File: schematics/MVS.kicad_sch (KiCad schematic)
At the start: 0 parts

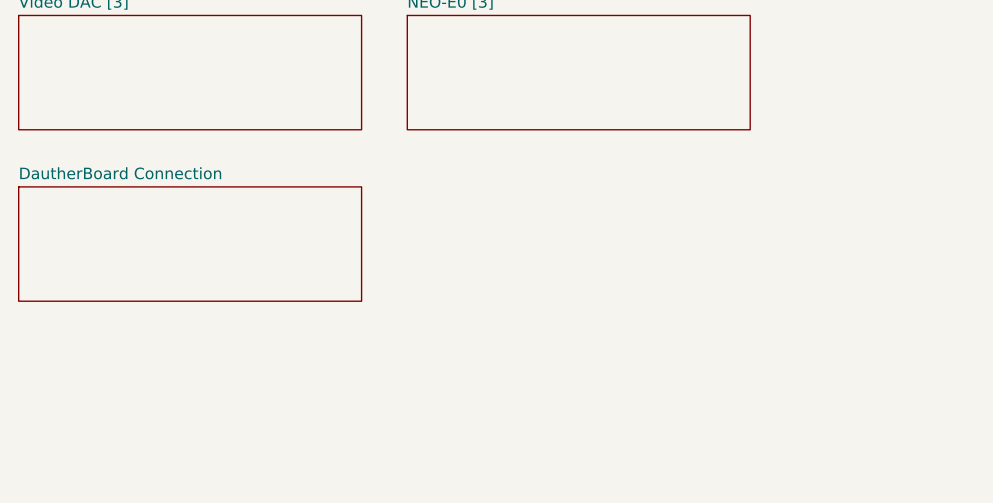
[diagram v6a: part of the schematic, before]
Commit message: complete DaughterBoard
rename sub files
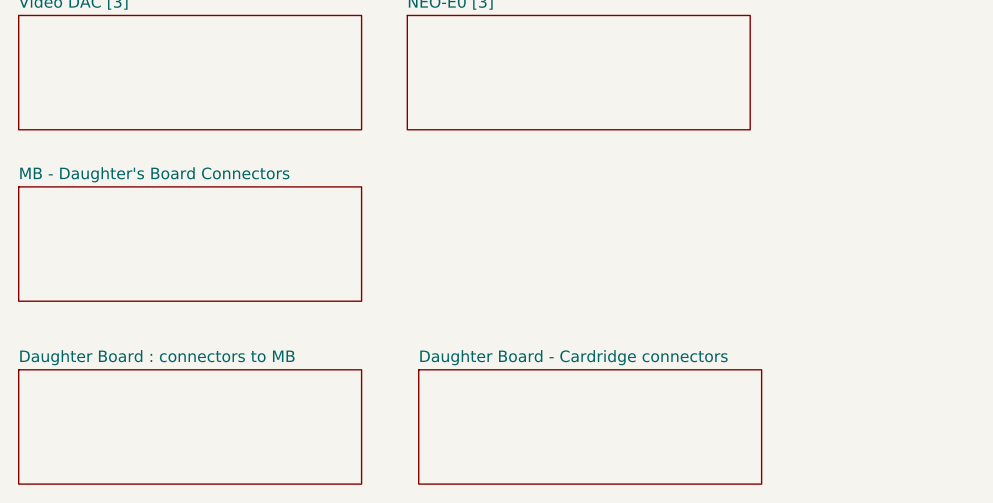
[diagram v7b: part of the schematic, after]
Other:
- sheet DautherBoard Connection renamed MB - Daughter's Board Connectors
- added sheet Daughter Board - Cardridge connectors (DB-Cardridge_Connectors.kicad_sch)
- added sheet Daughter Board : connectors to MB (daughterboard-MB-Connectors.kicad_sch)
- sheet 68K-SP ROM-Work & Back RAM [1]: file 68KWBRAM.kicad_sch -> MV1F-MB-68KWBRAM.kicad_sch
- sheet Audio [4]: file Audio.kicad_sch -> MV1F-MB-Audio.kicad_sch
- sheet Battery Circuit [1]: file BatterySaved.kicad_sch -> MV1F-MB-BatterySaved.kicad_sch
- sheet LSPC2-A2 & VRAM [3]: file lspc2-Vram.kicad_sch -> MV1F-MB-lspc2-Vram.kicad_sch
- sheet MB - Daughter's Board Connectors: file DaughterBoard.kicad_sch -> MV1F-MB-DB-Connectors.kicad_sch
- sheet NEO-C1 Players Input [1]: file PlayersInput.kicad_sch -> MV1F-MB-PlayersInput.kicad_sch
- sheet NEO-E0 [3]: file neo-e0-stuff.kicad_sch -> MV1F-MB-neo-e0-stuff.kicad_sch
- sheet UPD4990 Clock [1]: file clock.kicad_sch -> MV1F-MB-clock.kicad_sch
- sheet Video DAC [3]: file RGBDAC.kicad_sch -> MV1F-MB-RGBDAC.kicad_sch
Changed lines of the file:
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@@
       (effects (font (size 1.27 1.27)) (justify left bottom))
     )
-    (property "Sheetfile" "RGBDAC.kicad_sch" (at 25.4 88.2146 0)
+    (property "Sheetfile" "MV1F-MB-RGBDAC.kicad_sch" (at 25.4 88.2146 0)
       (effects (font (size 1.27 1.27)) (justify left top) hide)
     )
@@
       (effects (font (size 1.27 1.27)) (justify left bottom))
     )
-    (property "Sheetfile" "68KWBRAM.kicad_sch" (at 25.4 31.0646 0)
+    (property "Sheetfile" "MV1F-MB-68KWBRAM.kicad_sch" (at 25.4 31.0646 0)
       (effects (font (size 1.27 1.27)) (justify left top) hide)
     )
@@
       (effects (font (size 1.27 1.27)) (justify left bottom))
     )
-    (property "Sheetfile" "clock.kicad_sch" (at 25.4 69.1646 0)
+    (property "Sheetfile" "MV1F-MB-clock.kicad_sch" (at 25.4 69.1646 0)
       (effects (font (size 1.27 1.27)) (justify left top) hide)
     )
@@
       (effects (font (size 1.27 1.27)) (justify left bottom))
     )
-    (property "Sheetfile" "PlayersInput.kicad_sch" (at 25.4 50.1146 0)
+    (property "Sheetfile" "MV1F-MB-PlayersInput.kicad_sch" (at 25.4 50.1146 0)
       (effects (font (size 1.27 1.27)) (justify left top) hide)
     )
@@
       (project "MVS"
         (path "/8d0803ab-15ed-47a7-8dcb-ab27dc5b29c2" (page "3"))
+      )
+    )
+  )
+  (sheet (at 25.4 114.3) (size 38.1 12.7) (fields_autoplaced)
+    (stroke (width 0.1524) (type solid))
+    (fill (color 0 0 0 0.0000))
+    (property "Sheetname" "Daughter Board : connectors to MB" (at 25.4 113.5884 0)
+      (effects (font (size 1.27 1.27)) (justify left bottom))
+    )
+    (property "Sheetfile" "daughterboard-MB-Connectors.kicad_sch" (at 25.4 127.5846 0)
+      (effects (font (size 1.27 1.27)) (justify left top) hide)
+    )
+    (instances
+      (project "MVS"
+        (path "/8d0803ab-15ed-47a7-8dcb-ab27dc5b29c2" (page "12"))
       )
     )
@@
       (effects (font (size 1.27 1.27)) (justify left bottom))
     )
-    (property "Sheetfile" "lspc2-Vram.kicad_sch" (at 68.58 31.0646 0)
+    (property "Sheetfile" "MV1F-MB-lspc2-Vram.kicad_sch" (at 68.58 31.0646 0)
       (effects (font (size 1.27 1.27)) (justify left top) hide)
     )
@@
       (project "MVS"
         (path "/8d0803ab-15ed-47a7-8dcb-ab27dc5b29c2" (page "8"))
+      )
+    )
+  )
+  (sheet (at 69.85 114.3) (size 38.1 12.7) (fields_autoplaced)
+    (stroke (width 0.1524) (type solid))
+    (fill (color 0 0 0 0.0000))
+    (property "Sheetname" "Daughter Board - Cardridge connectors" (at 69.85 113.5884 0)
+      (effects (font (size 1.27 1.27)) (justify left bottom))
+    )
+    (property "Sheetfile" "DB-Cardridge_Connectors.kicad_sch" (at 69.85 127.5846 0)
+      (effects (font (size 1.27 1.27)) (justify left top) hide)
+    )
+    (instances
+      (project "MVS"
+        (path "/8d0803ab-15ed-47a7-8dcb-ab27dc5b29c2" (page "13"))
       )
     )
@@
       (effects (font (size 1.27 1.27)) (justify left bottom))
     )
-    (property "Sheetfile" "Audio.kicad_sch" (at 113.03 31.0646 0)
+    (property "Sheetfile" "MV1F-MB-Audio.kicad_sch" (at 113.03 31.0646 0) (show_name)
       (effects (font (size 1.27 1.27)) (justify left top) hide)
     )
@@
       (effects (font (size 1.27 1.27)) (justify left bottom))
     )
-    (property "Sheetfile" "BatterySaved.kicad_sch" (at 68.58 69.1646 0)
+    (property "Sheetfile" "MV1F-MB-BatterySaved.kicad_sch" (at 68.58 69.1646 0)
       (effects (font (size 1.27 1.27)) (justify left top) hide)
     )
@@
       (effects (font (size 1.27 1.27)) (justify left bottom))
     )
-    (property "Sheetfile" "neo-e0-stuff.kicad_sch" (at 68.58 88.2146 0)
+    (property "Sheetfile" "MV1F-MB-neo-e0-stuff.kicad_sch" (at 68.58 88.2146 0)
       (effects (font (size 1.27 1.27)) (justify left top) hide)
     )
@@
     (stroke (width 0.1524) (type solid))
     (fill (color 0 0 0 0.0000))
-    (property "Sheetname" "DautherBoard Connection" (at 25.4 93.2684 0)
+    (property "Sheetname" "MB - Daughter's Board Connectors" (at 25.4 93.2684 0)
       (effects (font (size 1.27 1.27)) (justify left bottom))
     )
-    (property "Sheetfile" "DaughterBoard.kicad_sch" (at 25.4 107.2646 0)
+    (property "Sheetfile" "MV1F-MB-DB-Connectors.kicad_sch" (at 25.4 107.2646 0)
       (effects (font (size 1.27 1.27)) (justify left top) hide)
     )

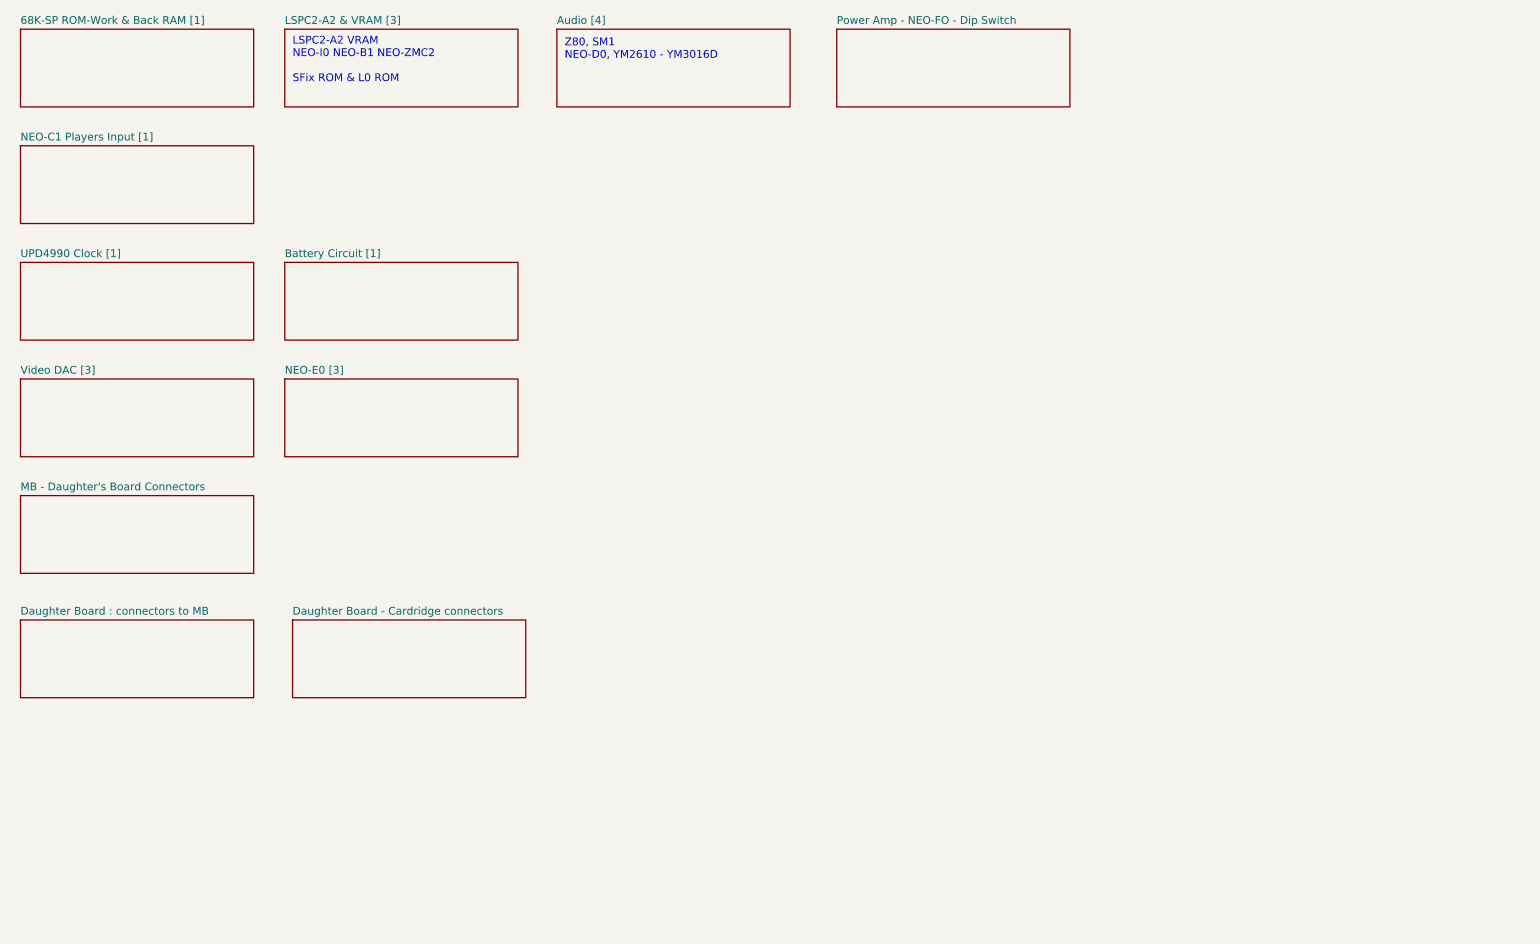
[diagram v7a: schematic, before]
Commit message: Typo... and orphan labels remove
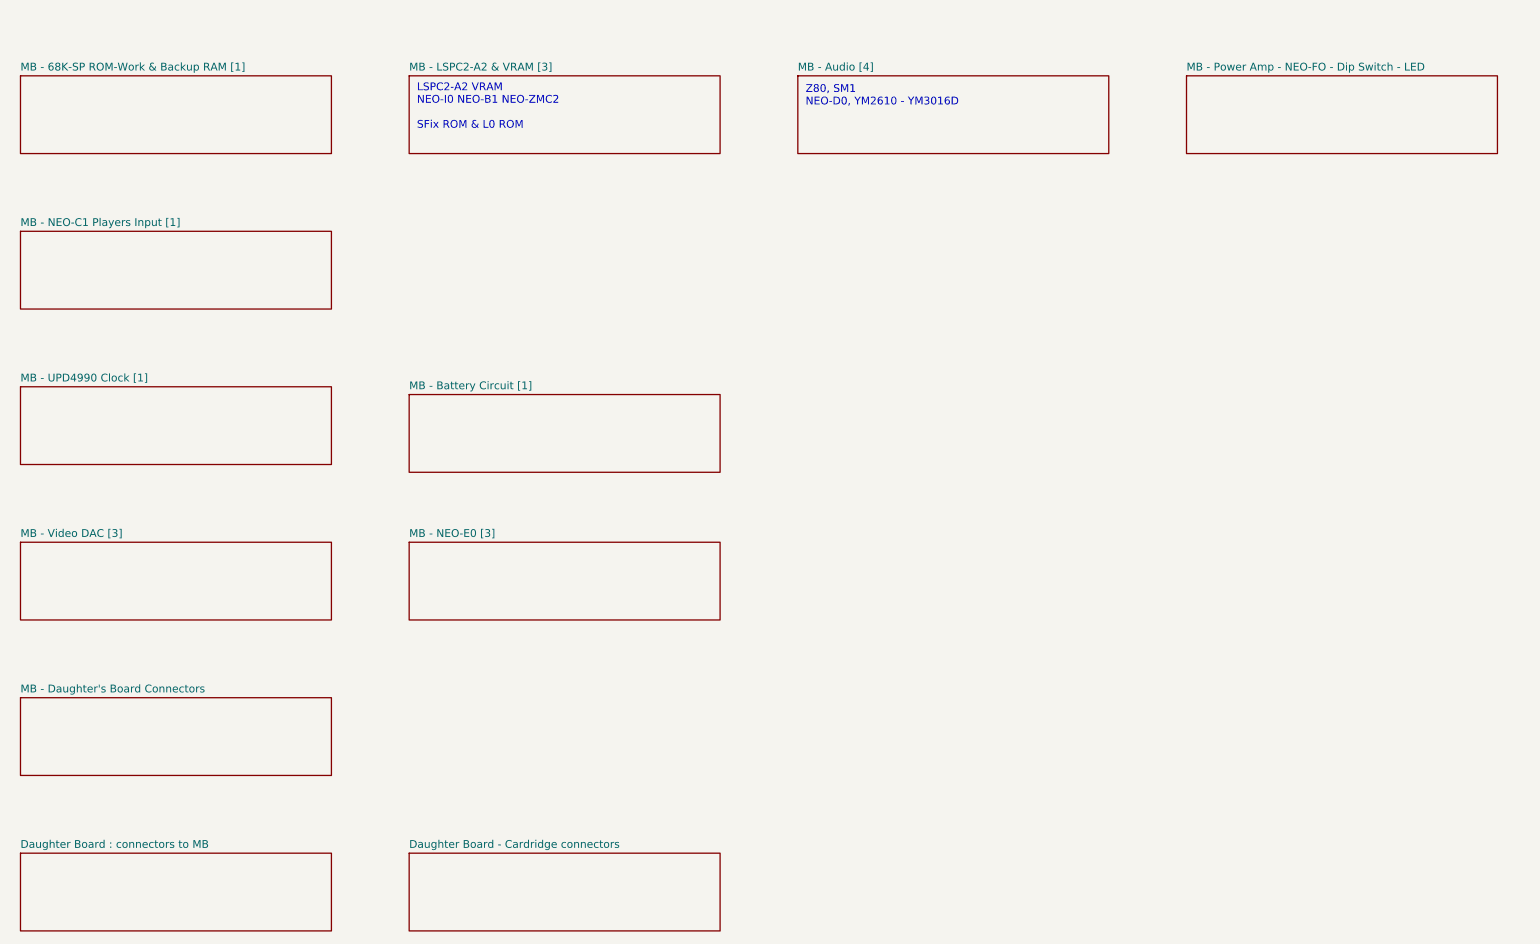
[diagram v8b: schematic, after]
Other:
- sheet 68K-SP ROM-Work & Back RAM [1] renamed MB - 68K-SP ROM-Work & Backup RAM [1]
- sheet Audio [4] renamed MB - Audio [4]
- sheet Battery Circuit [1] renamed MB - Battery Circuit [1]
- sheet LSPC2-A2 & VRAM [3] renamed MB - LSPC2-A2 & VRAM [3]
- sheet NEO-C1 Players Input [1] renamed MB - NEO-C1 Players Input [1]
- sheet NEO-E0 [3] renamed MB - NEO-E0 [3]
- sheet Power Amp - NEO-FO - Dip Switch renamed MB - Power Amp - NEO-FO - Dip Switch - LED
- sheet UPD4990 Clock [1] renamed MB - UPD4990 Clock [1]
- sheet Video DAC [3] renamed MB - Video DAC [3]
- sheet MB - Power Amp - NEO-FO - Dip Switch - LED: file PowerAmp-Neo-FO-Dip.kicad_sch -> MV1F-MB-PowerAmp-Neo-FO-Dip.kicad_sch
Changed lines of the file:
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@@
     (comment 9 "https://github.com/Neo-Geo-Hardwares/Schematics-MV1F")
   )
-  (text "Z80, SM1\nNEO-D0, YM2610 - YM3016D" (at 114.3 22.86 0)
+  (text "Z80, SM1\nNEO-D0, YM2610 - YM3016D" (at 153.67 30.48 0)
     (effects (font (size 1.27 1.27)) (justify left bottom))
   )
   (text "LSPC2-A2 VRAM \nNEO-I0 NEO-B1 NEO-ZMC2 \n\nSFix ROM & L0 ROM"
-    (at 69.85 26.67 0)
+    (at 90.17 34.29 0)
     (effects (font (size 1.27 1.27)) (justify left bottom))
   )
-  (sheet (at 25.4 74.93) (size 38.1 12.7) (fields_autoplaced)
+  (sheet (at 25.4 101.6) (size 50.8 12.7) (fields_autoplaced)
     (stroke (width 0.1524) (type solid))
     (fill (color 0 0 0 0.0000))
-    (property "Sheetname" "Video DAC [3]" (at 25.4 74.2184 0)
+    (property "Sheetname" "MB - Video DAC [3]" (at 25.4 100.8884 0)
       (effects (font (size 1.27 1.27)) (justify left bottom))
     )
-    (property "Sheetfile" "MV1F-MB-RGBDAC.kicad_sch" (at 25.4 88.2146 0)
+    (property "Sheetfile" "MV1F-MB-RGBDAC.kicad_sch" (at 25.4 114.8846 0)
       (effects (font (size 1.27 1.27)) (justify left top) hide)
     )
@@
     )
   )
-  (sheet (at 25.4 17.78) (size 38.1 12.7)
+  (sheet (at 25.4 25.4) (size 50.8 12.7)
     (stroke (width 0.1524) (type solid))
     (fill (color 0 0 0 0.0000))
-    (property "Sheetname" "68K-SP ROM-Work & Back RAM [1]" (at 25.4 17.0684 0)
+    (property "Sheetname" "MB - 68K-SP ROM-Work & Backup RAM [1]" (at 25.4 24.6884 0)
       (effects (font (size 1.27 1.27)) (justify left bottom))
     )
-    (property "Sheetfile" "MV1F-MB-68KWBRAM.kicad_sch" (at 25.4 31.0646 0)
+    (property "Sheetfile" "MV1F-MB-68KWBRAM.kicad_sch" (at 25.4 38.6846 0)
       (effects (font (size 1.27 1.27)) (justify left top) hide)
     )
@@
     )
   )
-  (sheet (at 158.75 17.78) (size 38.1 12.7) (fields_autoplaced)
+  (sheet (at 215.9 25.4) (size 50.8 12.7) (fields_autoplaced)
     (stroke (width 0.1524) (type solid))
     (fill (color 0 0 0 0.0000))
-    (property "Sheetname" "Power Amp - NEO-FO - Dip Switch" (at 158.75 17.0684 0)
+    (property "Sheetname" "MB - Power Amp - NEO-FO - Dip Switch - LED" (at 215.9 24.6884 0)
       (effects (font (size 1.27 1.27)) (justify left bottom))
     )
-    (property "Sheetfile" "PowerAmp-Neo-FO-Dip.kicad_sch" (at 158.75 31.0646 0)
+    (property "Sheetfile" "MV1F-MB-PowerAmp-Neo-FO-Dip.kicad_sch" (at 215.9 38.6846 0)
       (effects (font (size 1.27 1.27)) (justify left top) hide)
     )
@@
     )
   )
-  (sheet (at 25.4 55.88) (size 38.1 12.7) (fields_autoplaced)
+  (sheet (at 25.4 76.2) (size 50.8 12.7) (fields_autoplaced)
     (stroke (width 0.1524) (type solid))
     (fill (color 0 0 0 0.0000))
-    (property "Sheetname" "UPD4990 Clock [1]" (at 25.4 55.1684 0)
+    (property "Sheetname" "MB - UPD4990 Clock [1]" (at 25.4 75.4884 0)
       (effects (font (size 1.27 1.27)) (justify left bottom))
     )
-    (property "Sheetfile" "MV1F-MB-clock.kicad_sch" (at 25.4 69.1646 0)
+    (property "Sheetfile" "MV1F-MB-clock.kicad_sch" (at 25.4 89.4846 0)
       (effects (font (size 1.27 1.27)) (justify left top) hide)
     )
@@
     )
   )
-  (sheet (at 25.4 36.83) (size 38.1 12.7) (fields_autoplaced)
+  (sheet (at 25.4 50.8) (size 50.8 12.7) (fields_autoplaced)
     (stroke (width 0.1524) (type solid))
     (fill (color 0 0 0 0.0000))
-    (property "Sheetname" "NEO-C1 Players Input [1]" (at 25.4 36.1184 0)
+    (property "Sheetname" "MB - NEO-C1 Players Input [1]" (at 25.4 50.0884 0)
       (effects (font (size 1.27 1.27)) (justify left bottom))
     )
-    (property "Sheetfile" "MV1F-MB-PlayersInput.kicad_sch" (at 25.4 50.1146 0)
+    (property "Sheetfile" "MV1F-MB-PlayersInput.kicad_sch" (at 25.4 64.0846 0)
       (effects (font (size 1.27 1.27)) (justify left top) hide)
     )
@@
     )
   )
-  (sheet (at 25.4 114.3) (size 38.1 12.7) (fields_autoplaced)
+  (sheet (at 25.4 152.4) (size 50.8 12.7) (fields_autoplaced)
     (stroke (width 0.1524) (type solid))
     (fill (color 0 0 0 0.0000))
-    (property "Sheetname" "Daughter Board : connectors to MB" (at 25.4 113.5884 0)
+    (property "Sheetname" "Daughter Board : connectors to MB" (at 25.4 151.6884 0)
       (effects (font (size 1.27 1.27)) (justify left bottom))
     )
-    (property "Sheetfile" "daughterboard-MB-Connectors.kicad_sch" (at 25.4 127.5846 0)
+    (property "Sheetfile" "daughterboard-MB-Connectors.kicad_sch" (at 25.4 165.6846 0)
       (effects (font (size 1.27 1.27)) (justify left top) hide)
     )
@@
     )
   )
-  (sheet (at 68.58 17.78) (size 38.1 12.7)
+  (sheet (at 88.9 25.4) (size 50.8 12.7)
     (stroke (width 0.1524) (type solid))
     (fill (color 0 0 0 0.0000))
-    (property "Sheetname" "LSPC2-A2 & VRAM [3]" (at 68.58 17.0684 0)
+    (property "Sheetname" "MB - LSPC2-A2 & VRAM [3]" (at 88.9 24.6884 0)
       (effects (font (size 1.27 1.27)) (justify left bottom))
     )
-    (property "Sheetfile" "MV1F-MB-lspc2-Vram.kicad_sch" (at 68.58 31.0646 0)
+    (property "Sheetfile" "MV1F-MB-lspc2-Vram.kicad_sch" (at 88.9 38.6846 0)
       (effects (font (size 1.27 1.27)) (justify left top) hide)
     )
@@
     )
   )
-  (sheet (at 69.85 114.3) (size 38.1 12.7) (fields_autoplaced)
+  (sheet (at 88.9 152.4) (size 50.8 12.7) (fields_autoplaced)
     (stroke (width 0.1524) (type solid))
     (fill (color 0 0 0 0.0000))
-    (property "Sheetname" "Daughter Board - Cardridge connectors" (at 69.85 113.5884 0)
+    (property "Sheetname" "Daughter Board - Cardridge connectors" (at 88.9 151.6884 0)
       (effects (font (size 1.27 1.27)) (justify left bottom))
     )
-    (property "Sheetfile" "DB-Cardridge_Connectors.kicad_sch" (at 69.85 127.5846 0)
+    (property "Sheetfile" "DB-Cardridge_Connectors.kicad_sch" (at 88.9 165.6846 0)
       (effects (font (size 1.27 1.27)) (justify left top) hide)
     )
@@
     )
   )
-  (sheet (at 113.03 17.78) (size 38.1 12.7) (fields_autoplaced)
+  (sheet (at 152.4 25.4) (size 50.8 12.7) (fields_autoplaced)
     (stroke (width 0.1524) (type solid))
     (fill (color 0 0 0 0.0000))
-    (property "Sheetname" "Audio [4]" (at 113.03 17.0684 0)
+    (property "Sheetname" "MB - Audio [4]" (at 152.4 24.6884 0)
       (effects (font (size 1.27 1.27)) (justify left bottom))
     )
-    (property "Sheetfile" "MV1F-MB-Audio.kicad_sch" (at 113.03 31.0646 0) (show_name)
+    (property "Sheetfile" "MV1F-MB-Audio.kicad_sch" (at 152.4 38.6846 0) (show_name)
       (effects (font (size 1.27 1.27)) (justify left top) hide)
     )
@@
     )
   )
-  (sheet (at 68.58 55.88) (size 38.1 12.7) (fields_autoplaced)
+  (sheet (at 88.9 77.47) (size 50.8 12.7) (fields_autoplaced)
     (stroke (width 0.1524) (type solid))
     (fill (color 0 0 0 0.0000))
-    (property "Sheetname" "Battery Circuit [1]" (at 68.58 55.1684 0)
+    (property "Sheetname" "MB - Battery Circuit [1]" (at 88.9 76.7584 0)
       (effects (font (size 1.27 1.27)) (justify left bottom))
     )
-    (property "Sheetfile" "MV1F-MB-BatterySaved.kicad_sch" (at 68.58 69.1646 0)
+    (property "Sheetfile" "MV1F-MB-BatterySaved.kicad_sch" (at 88.9 90.7546 0)
       (effects (font (size 1.27 1.27)) (justify left top) hide)
     )
@@
     )
   )
-  (sheet (at 68.58 74.93) (size 38.1 12.7) (fields_autoplaced)
+  (sheet (at 88.9 101.6) (size 50.8 12.7) (fields_autoplaced)
     (stroke (width 0.1524) (type solid))
     (fill (color 0 0 0 0.0000))
-    (property "Sheetname" "NEO-E0 [3]" (at 68.58 74.2184 0)
+    (property "Sheetname" "MB - NEO-E0 [3]" (at 88.9 100.8884 0)
       (effects (font (size 1.27 1.27)) (justify left bottom))
     )
-    (property "Sheetfile" "MV1F-MB-neo-e0-stuff.kicad_sch" (at 68.58 88.2146 0)
+    (property "Sheetfile" "MV1F-MB-neo-e0-stuff.kicad_sch" (at 88.9 114.8846 0)
       (effects (font (size 1.27 1.27)) (justify left top) hide)
     )
@@
     )
   )
-  (sheet (at 25.4 93.98) (size 38.1 12.7) (fields_autoplaced)
+  (sheet (at 25.4 127) (size 50.8 12.7) (fields_autoplaced)
     (stroke (width 0.1524) (type solid))
     (fill (color 0 0 0 0.0000))
-    (property "Sheetname" "MB - Daughter's Board Connectors" (at 25.4 93.2684 0)
+    (property "Sheetname" "MB - Daughter's Board Connectors" (at 25.4 126.2884 0)
       (effects (font (size 1.27 1.27)) (justify left bottom))
     )
-    (property "Sheetfile" "MV1F-MB-DB-Connectors.kicad_sch" (at 25.4 107.2646 0)
+    (property "Sheetfile" "MV1F-MB-DB-Connectors.kicad_sch" (at 25.4 140.2846 0)
       (effects (font (size 1.27 1.27)) (justify left top) hide)
     )
